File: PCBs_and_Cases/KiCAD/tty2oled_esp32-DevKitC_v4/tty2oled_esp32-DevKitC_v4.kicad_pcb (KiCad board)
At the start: 2 copper layers, 35.6 x 99.7 mm, 2 parts

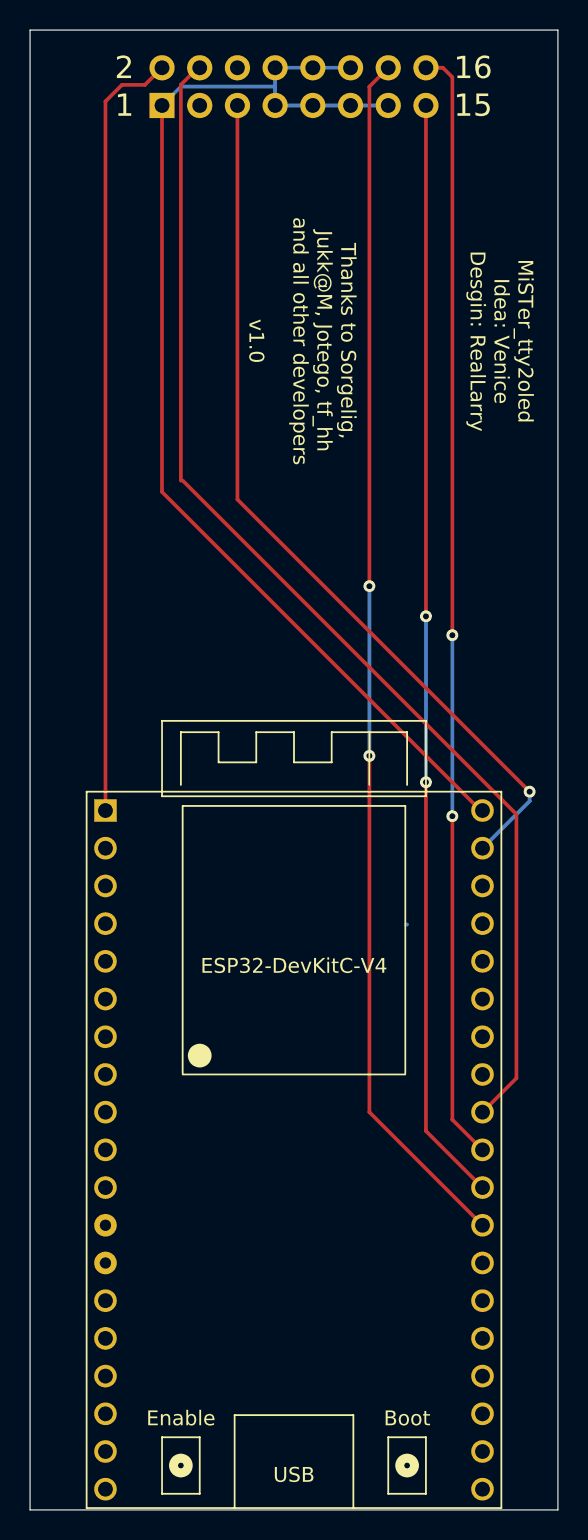
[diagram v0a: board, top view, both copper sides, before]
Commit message: Update board esp32-DevKitC to v1.1
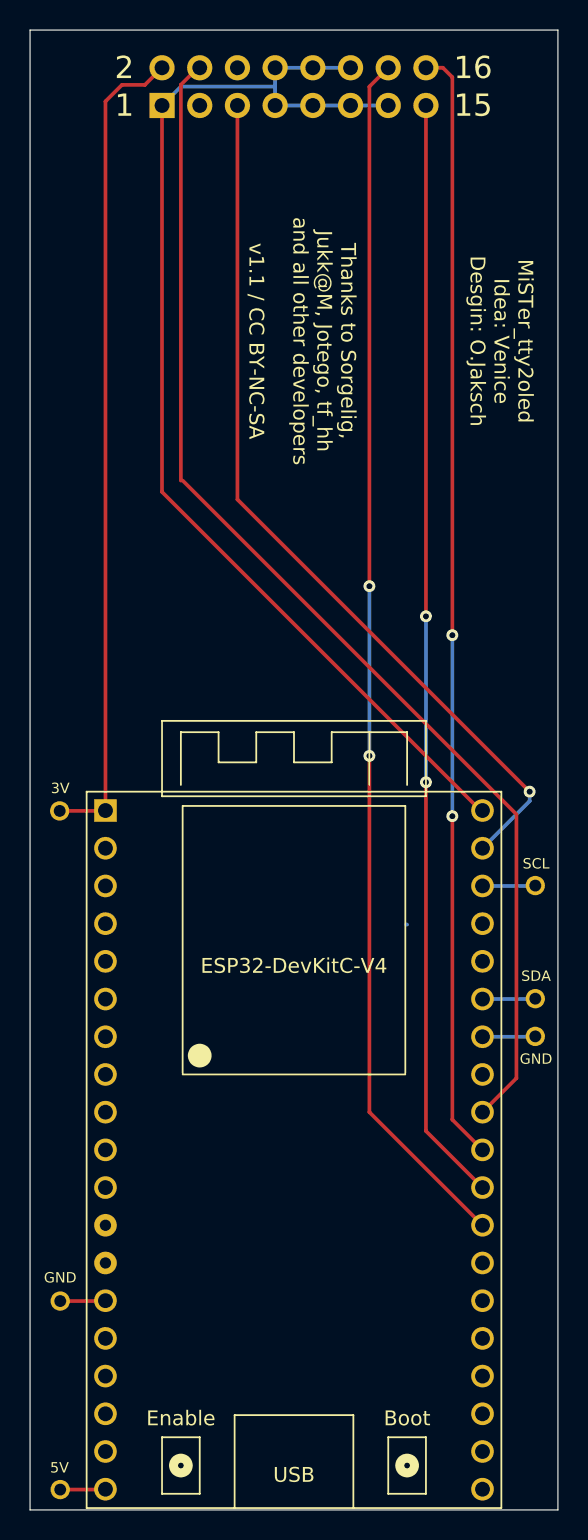
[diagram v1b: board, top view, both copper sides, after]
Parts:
- added REF**: SolderWirePad_single_0-8mmDrill, Wire_Pads:SolderWirePad_single_0-8mmDrill, F.Cu at (166.1, 116.7)
- added REF**: SolderWirePad_single_0-8mmDrill, Wire_Pads:SolderWirePad_single_0-8mmDrill, F.Cu at (166.1, 109.1)
- added REF**: SolderWirePad_single_0-8mmDrill, Wire_Pads:SolderWirePad_single_0-8mmDrill, F.Cu at (166.1, 119.2)
- added REF**: SolderWirePad_single_0-8mmDrill, Wire_Pads:SolderWirePad_single_0-8mmDrill, F.Cu at (134.1, 137.1)
- added REF**: SolderWirePad_single_0-8mmDrill, Wire_Pads:SolderWirePad_single_0-8mmDrill, F.Cu at (134.1, 149.8)
- added REF**: SolderWirePad_single_0-8mmDrill, Wire_Pads:SolderWirePad_single_0-8mmDrill, F.Cu at (134.1, 104.0)
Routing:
- net (no net): track 504.5 -> 524.5 mm
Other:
- board text added: "3V"
- board text added: "5V"
- board text added: "GND"
- board text added: "MiSTer_tty2oled Idea: Venice Desgin: O.Jaksch"
- board text added: "SCL"
- board text added: "SDA"
- board text added: "v1.1 / CC BY-NC-SA"
- board text removed: "MiSTer_tty2oled Idea: Venice Desgin: RealLarry"
- board text removed: "v1.0"
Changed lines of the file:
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@@
   (general
     (thickness 1.6)
-    (drawings 12)
-    (tracks 48)
+    (drawings 17)
+    (tracks 60)
     (zones 0)
-    (modules 2)
+    (modules 8)
     (nets 1)
   )
@@
     (mod_text_size 1 1)
     (mod_text_width 0.15)
-    (pad_size 1.524 1.524)
-    (pad_drill 1)
+    (pad_size 1.3 1.3)
+    (pad_drill 0.8001)
     (pad_to_mask_clearance 0)
     (aux_axis_origin 132.08 151.13)
@@
     (uvia_dia 0.3)
     (uvia_drill 0.1)
+  )
+  (module Wire_Pads:SolderWirePad_single_0-8mmDrill (layer F.Cu)
+    (at 166.116 116.6876)
+    (fp_text reference REF** (at 0 -2.54) (layer F.SilkS) hide
+      (effects (font (size 1 1) (thickness 0.15)))
+    )
+    (fp_text value SolderWirePad_single_0-8mmDrill (at 0 2.54) (layer F.Fab) hide
+      (effects (font (size 1 1) (thickness 0.15)))
+    )
+    (pad 1 thru_hole circle (at 0 0) (size 1.3 1.3) (drill 0.8001) (layers *.Cu *.Mask))
+  )
+  (module Wire_Pads:SolderWirePad_single_0-8mmDrill (layer F.Cu)
+    (at 166.116 109.0676)
+    (fp_text reference REF** (at 0 -2.54) (layer F.SilkS) hide
+      (effects (font (size 1 1) (thickness 0.15)))
+    )
+    (fp_text value SolderWirePad_single_0-8mmDrill (at 0 2.54) (layer F.Fab) hide
+      (effects (font (size 1 1) (thickness 0.15)))
+    )
+    (pad 1 thru_hole circle (at 0 0) (size 1.3 1.3) (drill 0.8001) (layers *.Cu *.Mask))
+  )
+  (module Wire_Pads:SolderWirePad_single_0-8mmDrill (layer F.Cu)
+    (at 166.116 119.2276)
+    (fp_text reference REF** (at 0 -2.54) (layer F.SilkS) hide
+      (effects (font (size 1 1) (thickness 0.15)))
+    )
+    (fp_text value SolderWirePad_single_0-8mmDrill (at 0 2.54) (layer F.Fab) hide
+      (effects (font (size 1 1) (thickness 0.15)))
+    )
+    (pad 1 thru_hole circle (at 0 0) (size 1.3 1.3) (drill 0.8001) (layers *.Cu *.Mask))
+  )
+  (module Wire_Pads:SolderWirePad_single_0-8mmDrill (layer F.Cu)
+    (at 134.112 137.0584)
+    (fp_text reference REF** (at 0 -2.54) (layer F.SilkS) hide
+      (effects (font (size 1 1) (thickness 0.15)))
+    )
+    (fp_text value SolderWirePad_single_0-8mmDrill (at 0 2.54) (layer F.Fab) hide
+      (effects (font (size 1 1) (thickness 0.15)))
+    )
+    (pad 1 thru_hole circle (at 0 0) (size 1.3 1.3) (drill 0.8001) (layers *.Cu *.Mask))
+  )
+  (module Wire_Pads:SolderWirePad_single_0-8mmDrill (layer F.Cu)
+    (at 134.112 149.7584)
+    (fp_text reference REF** (at 0 -2.54) (layer F.SilkS) hide
+      (effects (font (size 1 1) (thickness 0.15)))
+    )
+    (fp_text value SolderWirePad_single_0-8mmDrill (at 0 2.54) (layer F.Fab) hide
+      (effects (font (size 1 1) (thickness 0.15)))
+    )
+    (pad 1 thru_hole circle (at 0 0) (size 1.3 1.3) (drill 0.8001) (layers *.Cu *.Mask))
+  )
+  (module Wire_Pads:SolderWirePad_single_0-8mmDrill (layer F.Cu)
+    (at 134.07644 104.0384)
+    (fp_text reference REF** (at 0 -2.54) (layer F.SilkS) hide
+      (effects (font (size 1 1) (thickness 0.15)))
+    )
+    (fp_text value SolderWirePad_single_0-8mmDrill (at 0 2.54) (layer F.Fab) hide
+      (effects (font (size 1 1) (thickness 0.15)))
+    )
+    (pad 1 thru_hole circle (at 0 0) (size 1.3 1.3) (drill 0.8001) (layers *.Cu *.Mask))
   )
   (module _my_footprints:esp32_devkit_v4 (layer F.Cu)
@@
     )
   )
+  (gr_text GND (at 166.1668 120.7516) (layer F.SilkS)
+    (effects (font (size 0.7 0.7) (thickness 0.15)))
+  )
+  (gr_text SDA (at 166.1668 115.1636) (layer F.SilkS)
+    (effects (font (size 0.7 0.7) (thickness 0.15)))
+  )
+  (gr_text SCL (at 166.1668 107.5944) (layer F.SilkS)
+    (effects (font (size 0.7 0.7) (thickness 0.15)))
+  )
+  (gr_text 5V (at 134.0612 148.2852) (layer F.SilkS)
+    (effects (font (size 0.7 0.7) (thickness 0.15)))
+  )
+  (gr_text GND (at 134.112 135.4836) (layer F.SilkS)
+    (effects (font (size 0.7 0.7) (thickness 0.15)))
+  )
+  (gr_text 3V (at 134.112 102.5144) (layer F.SilkS)
+    (effects (font (size 0.7 0.7) (thickness 0.15)))
+  )
   (gr_text "Thanks to Sorgelig,\nJukk@M, Jotego, tf_hh\nand all other developers" (at 151.892 72.39 -90) (layer F.SilkS)
     (effects (font (size 1 1) (thickness 0.15)))
   )
-  (gr_text v1.0 (at 147.32 72.39 -90) (layer F.SilkS)
+  (gr_text "v1.1 / CC BY-NC-SA" (at 147.32 72.39 -90) (layer F.SilkS)
     (effects (font (size 1 1) (thickness 0.15)))
   )
-  (gr_text "MiSTer_tty2oled\nIdea: Venice\nDesgin: RealLarry" (at 163.83 72.39 -90) (layer F.SilkS)
+  (gr_text "MiSTer_tty2oled\nIdea: Venice\nDesgin: O.Jaksch" (at 163.83 72.39 -90) (layer F.SilkS)
     (effects (font (size 1 1) (thickness 0.15)))
   )
@@
   (gr_line (start 167.64 51.435) (end 132.08 51.435) (layer Edge.Cuts) (width 0.05))
   (gr_line (start 132.08 151.13) (end 167.64 151.13) (layer Edge.Cuts) (width 0.05))
-  (target plus (at 132.08 151.13) (size 5) (width 0.05) (layer Edge.Cuts))
   (gr_text 16 (at 161.925 53.975) (layer F.SilkS)
     (effects (font (size 1.5 1.5) (thickness 0.3)))
@@
   (segment (start 160.528 104.394) (end 160.528 124.841) (width 0.25) (layer F.Cu) (net 0))
   (via (at 160.528 104.394) (size 0.8) (drill 0.4) (layers F.Cu B.Cu) (net 0))
+  (segment (start 166.0906 116.713) (end 166.116 116.6876) (width 0.25) (layer B.Cu) (net 0))
+  (segment (start 162.56 116.713) (end 166.0906 116.713) (width 0.25) (layer B.Cu) (net 0))
+  (segment (start 166.0906 119.253) (end 166.116 119.2276) (width 0.25) (layer B.Cu) (net 0))
+  (segment (start 162.56 119.253) (end 166.0906 119.253) (width 0.25) (layer B.Cu) (net 0))
+  (segment (start 166.0906 109.093) (end 166.116 109.0676) (width 0.25) (layer B.Cu) (net 0))
+  (segment (start 162.56 109.093) (end 166.0906 109.093) (width 0.25) (layer B.Cu) (net 0))
+  (segment (start 137.1346 104.0384) (end 137.16 104.013) (width 0.25) (layer B.Cu) (net 0))
+  (segment (start 134.07644 104.0384) (end 137.1346 104.0384) (width 0.25) (layer F.Cu) (net 0))
+  (segment (start 137.1346 137.0584) (end 137.16 137.033) (width 0.25) (layer B.Cu) (net 0))
+  (segment (start 134.112 137.0584) (end 137.1346 137.0584) (width 0.25) (layer F.Cu) (net 0))
+  (segment (start 137.1346 149.7584) (end 137.16 149.733) (width 0.25) (layer B.Cu) (net 0))
+  (segment (start 134.112 149.7584) (end 137.1346 149.7584) (width 0.25) (layer F.Cu) (net 0))
 )
